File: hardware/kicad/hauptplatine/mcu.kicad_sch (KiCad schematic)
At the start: 38 parts, among them J301 Laden 5 V, J302 Debug (SWD + Serial1), Q301 AO3401A, SW301 Reset, SW302 BOOT, SW303 Service, SW304 MRS03-B-3, U301 STM32F411CEU6, U303 RN4871-I/RM130, Y301 25MHz 12pF, Y302 32,768k 7pF

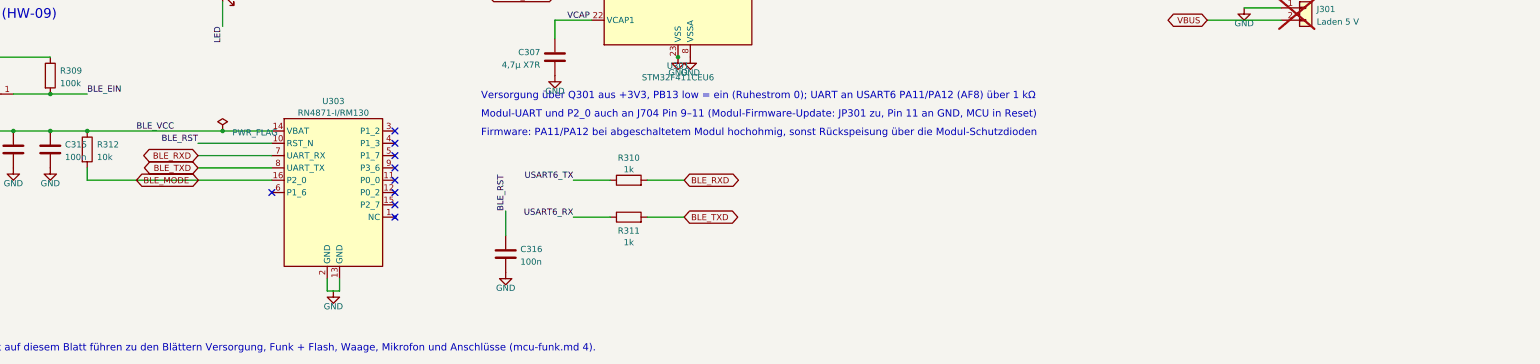
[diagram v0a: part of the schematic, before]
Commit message: Review-Nachtrag: mikrofon.md J601 Pin 5/6 berichtigt, Q501 ohne unverifizierte LCSC-Nummer, R313 Entladung BLE_VCC
Netzpruefung 230/230, ERC 0, Pin/Footprint 186/0. PDF noch nicht neu erzeugt (Datei durch einen Viewer gesperrt).

Co-Authored-By: Claude Fable 5.1 <noreply@anthropic.com>
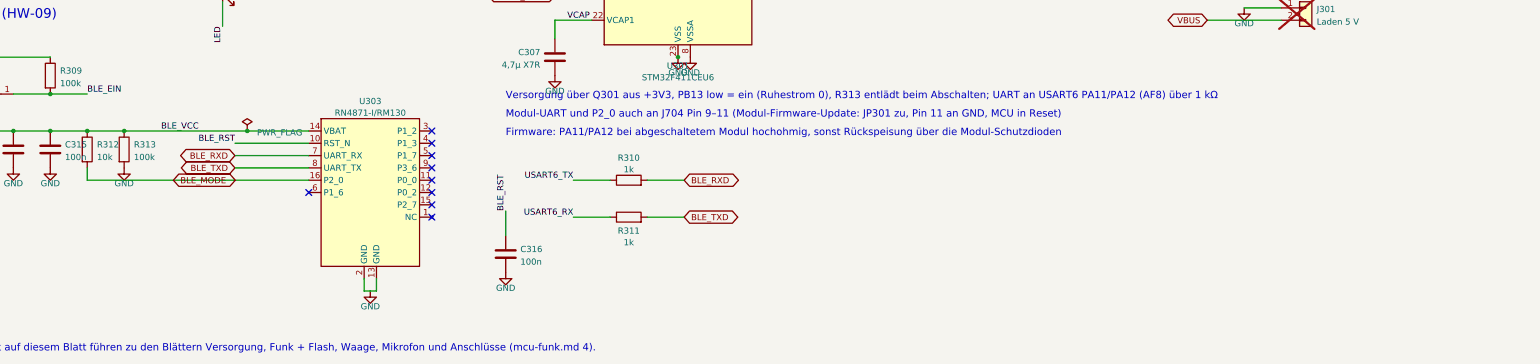
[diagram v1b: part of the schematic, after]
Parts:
- added R313: 100k, Resistor_SMD:R_0603_1608Metric, symbol Device:R
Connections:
- net BLE_VCC: now also R313.1
- net GND: now also R313.2
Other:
- note added: "Versorgung über Q301 aus +3V3, PB13 low = ein (Ruhestrom 0), R313 entlädt beim Abschalten; UART an USART6 PA11/PA12 (AF8) über 1 kΩ"
- note removed: "Versorgung über Q301 aus +3V3, PB13 low = ein (Ruhestrom 0); UART an USART6 PA11/PA12 (AF8) über 1 kΩ"
- moved on the sheet: U303

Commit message: HW-11: sechs Bauteile entfallen (R302, C308, FB301, C306, R407, R408), Sanftanlauf R314/C317 am BLE-Lastschalter
Philipp: sichere Streichungen und Sanftanlauf ja, 5-V-Wandler der Waage bleibt. PB2 direkt GND, VBAT ohne
eigenen C, VDDA direkt an +3V3 (C305), Flash WP/HOLD direkt an +3V3; drei begruendete ERC-Warnungen
(pin_to_pin) in erc_erwartet.json. Netzpruefung 237/237, Pin/Footprint 182/0, SPICE 12/12 (S3: 55 mA, 3,29 V).

Co-Authored-By: Claude Fable 5.1 <noreply@anthropic.com>
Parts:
- removed C306: 1µ, Capacitor_SMD:C_0603_1608Metric, symbol Device:C
- removed C308: 100n, Capacitor_SMD:C_0603_1608Metric, symbol Device:C
- removed FB301: 600R@100MHz, Inductor_SMD:L_0603_1608Metric, symbol Device:FerriteBead_Small
- removed R302: 10k, Resistor_SMD:R_0603_1608Metric, symbol Device:R
- added C317: 47n, Capacitor_SMD:C_0603_1608Metric, symbol Device:C
- added R314: 10k, Resistor_SMD:R_0603_1608Metric, symbol Device:R
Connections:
- net BOOT1 is gone; now on net GND: U301.20 (PB2)
- net VDDA is gone; now on net +3V3: C305.1, U301.9 (VDDA)
- net BLE_EIN: now also R314.2; no longer Q301.1 (G), R309.2
- net BLE_VCC: now also C317.2
- new net BLE_GATE: C317.1, Q301.1 (G), R309.2, R314.1
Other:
- note added: "1 Versorgung: VDD je 100 nF am Pin, VDDA und VBAT direkt an 3,3 V (HW-11), VCAP 4,7 µF"
- note added: "Versorgung über Q301 aus +3V3, PB13 low = ein (Ruhestrom 0), Sanftanlauf R314/C317, R313 entlädt beim Abschalten; UART an USART6 PA11/PA12 (AF8) über 1 kΩ"
- note removed: "1 Versorgung: VDD je 100 nF am Pin, VDDA über Ferrit, VBAT an 3,3 V, VCAP 4,7 µF"
- note removed: "Versorgung über Q301 aus +3V3, PB13 low = ein (Ruhestrom 0), R313 entlädt beim Abschalten; UART an USART6 PA11/PA12 (AF8) über 1 kΩ"
- moved on the sheet: C305
